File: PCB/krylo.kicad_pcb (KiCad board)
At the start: 2 copper layers, 135.3 x 87.6 mm, 51 parts, among them SW1 Switch, SW10 Switch, SW11 Switch, SW12 Switch, SW13 Switch, SW14 Switch, SW15 Switch, SW16 Switch, SW2 Switch, SW3 Switch, SW4 Switch, SW5 Switch, SW6 Switch, SW7 Switch, SW8 Switch, SW9 Switch, U1 nice_nano

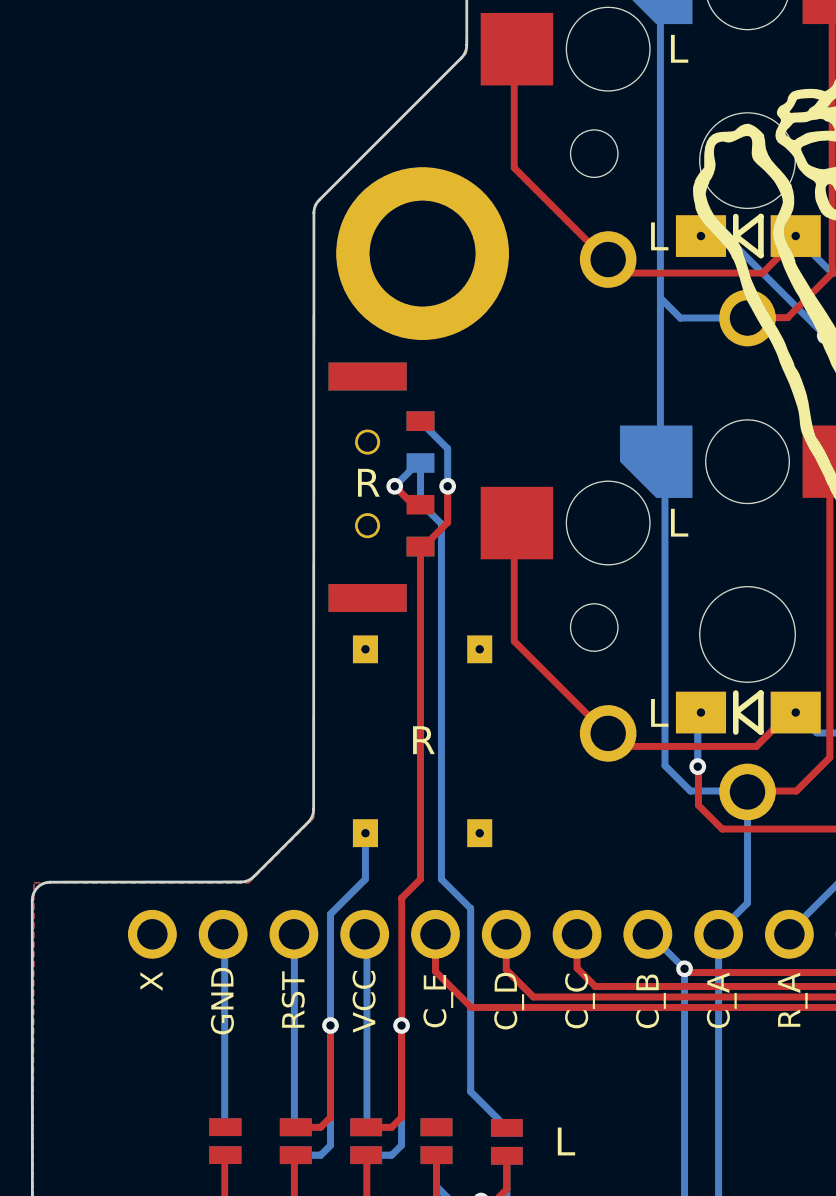
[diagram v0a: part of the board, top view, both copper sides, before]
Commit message: Repositioned the reset button and the mount point to make them a bit more centered relative to the resulting area
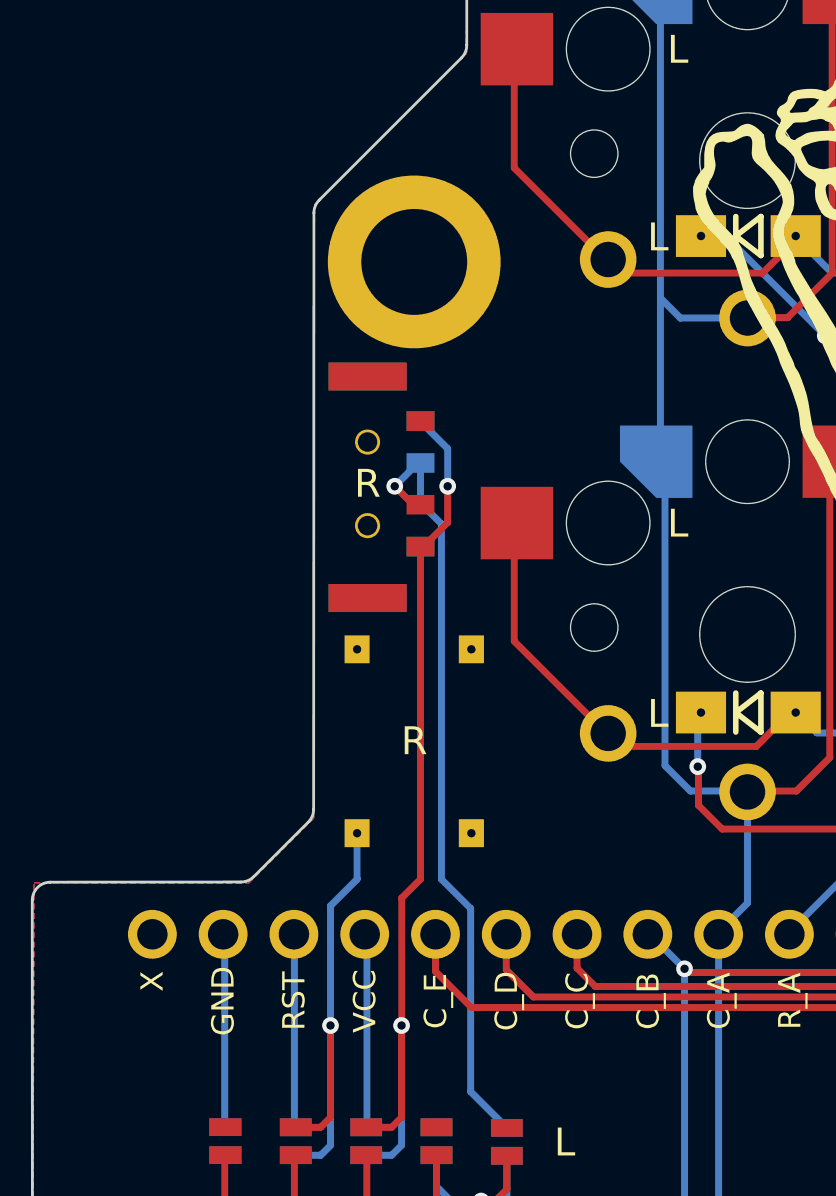
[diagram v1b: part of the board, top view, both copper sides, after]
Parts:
- moved H4 0.42 mm to (105.0, 74.2)
- moved RESET1 0.30 mm to (105.0, 91.4)
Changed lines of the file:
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@@
 		(fp_poly
 			(pts
-				(xy -8.75 -8.250001) (xy 8.75 -8.25) (xy 8.75 8.250001) (xy -8.75 8.25)
+				(xy -8.75 -8.250002) (xy 8.75 -8.25) (xy 8.75 8.250002) (xy -8.75 8.25)
 			)
 			(stroke
@@
 		(fp_poly
 			(pts
-				(xy -8.75 -8.250001) (xy 8.75 -8.25) (xy 8.75 8.250001) (xy -8.75 8.25)
+				(xy -8.75 -8.250002) (xy 8.75 -8.25) (xy 8.75 8.250002) (xy -8.75 8.25)
 			)
 			(stroke
@@
 		(fp_line
 			(start 2.5 -1.5)
-			(end 7.000001 -1.5)
+			(end 7.000002 -1.5)
 			(stroke
 				(width 0.1)
@@
 		)
 		(fp_line
-			(start 7.000001 -1.5)
+			(start 7.000002 -1.5)
 			(end 7 -6.2)
 			(stroke
@@
 		)
 		(fp_line
-			(start -9.55 -2.499999)
+			(start -9.55 -2.499998)
 			(end -7 -2.5)
 			(stroke
@@
 		(fp_line
 			(start -9.55 -5)
-			(end -9.55 -2.499999)
+			(end -9.55 -2.499998)
 			(stroke
 				(width 0.1)
@@
 		)
 		(fp_line
-			(start 4.549999 -5.957)
+			(start 4.549998 -5.957)
 			(end 4.55 -7.228)
 			(stroke
@@
 		)
 		(fp_line
-			(start -9.549999 -2.5)
+			(start -9.549998 -2.5)
 			(end -7 -2.5)
 			(stroke
@@
 		(fp_line
 			(start -9.55 -5)
-			(end -9.549999 -2.5)
+			(end -9.549998 -2.5)
 			(stroke
 				(width 0.1)
@@
 		)
 		(fp_line
-			(start -9.549999 -2.5)
+			(start -9.549998 -2.5)
 			(end -7 -2.5)
 			(stroke
@@
 		(fp_line
 			(start -9.55 -5)
-			(end -9.549999 -2.5)
+			(end -9.549998 -2.5)
 			(stroke
 				(width 0.1)
@@
 		)
 		(fp_line
-			(start -9.549999 -2.5)
+			(start -9.549998 -2.5)
 			(end -7 -2.5)
 			(stroke
@@
 		(fp_line
 			(start -9.55 -5)
-			(end -9.549999 -2.5)
+			(end -9.549998 -2.5)
 			(stroke
 				(width 0.1)
@@
 		(fp_line
 			(start -2 -7.7)
-			(end -1.5 -8.200001)
+			(end -1.5 -8.200002)
 			(stroke
 				(width 0.1)
@@
 		)
 		(fp_line
-			(start -1.5 -8.200001)
+			(start -1.5 -8.200002)
 			(end 1.5 -8.2)
 			(stroke
@@
 		(fp_line
 			(start 7 -5)
-			(end 9.55 -4.999999)
+			(end 9.55 -4.999998)
 			(stroke
 				(width 0.1)
@@
 		)
 		(fp_line
-			(start 9.55 -4.999999)
+			(start 9.55 -4.999998)
 			(end 9.55 -2.5)
 			(stroke
@@
 		)
 		(fp_line
-			(start -1.5 -8.200001)
+			(start -1.5 -8.200002)
 			(end -2 -7.7)
 			(stroke
@@
 		(fp_line
 			(start 1.5 -8.2)
-			(end -1.5 -8.200001)
+			(end -1.5 -8.200002)
 			(stroke
 				(width 0.1)
@@
 		)
 		(fp_line
-			(start 1.999999 -4.25)
+			(start 1.999998 -4.25)
 			(end 2 -7.7)
 			(stroke
@@
 		(fp_line
 			(start 4.54 -5.95)
-			(end 3.281 -4.690999)
+			(end 3.281 -4.690998)
 			(stroke
 				(width 0.1)
@@
 	(footprint "krylo:Mount"
 		(layer "F.Cu")
-		(at 105.3 73.9)
+		(at 105 74.2)
 		(property "Reference" "H4"
 			(at 0 -2.5 0)
@@
 	(footprint "krylo:ResetSW"
 		(layer "F.Cu")
-		(at 105.3 91.4 -90)
+		(at 105 91.4 -90)
 		(descr "tactile push button, 6x6mm e.g. PTS645xx series, height=9.5mm")
 		(tags "tact sw push 6mm smd")
@@
 				(polygon
 					(pts
-						(xy 105.37209 90.79822) (xy 105.434574 90.81107) (xy 105.488983 90.831495) (xy 105.538795 90.860676)
-						(xy 105.579725 90.896447) (xy 105.612753 90.939206) (xy 105.636843 90.987586) (xy 105.651679 91.04217)
-						(xy 105.656839 91.104314) (xy 105.651307 91.169119) (xy 105.635164 91.227962) (xy 105.608539 91.282001)
-						(xy 105.572257 91.329736) (xy 105.528931 91.367188) (xy 105.477747 91.395268) (xy 105.670821 91.815)
-						(xy 105.442821 91.815) (xy 105.277713 91.428852) (xy 105.179771 91.428852) (xy 105.179771 91.815)
-						(xy 104.972714 91.815) (xy 104.972714 91.247013) (xy 105.179771 91.247013) (xy 105.300122 91.247013)
-						(xy 105.345474 91.242672) (xy 105.380867 91.230735) (xy 105.408505 91.212025) (xy 105.429415 91.186381)
-						(xy 105.44235 91.154369) (xy 105.446973 91.114084) (xy 105.442312 91.071869) (xy 105.429331 91.038512)
-						(xy 105.408505 91.01199) (xy 105.380756 90.992472) (xy 105.345361 90.980089) (xy 105.300122 90.975598)
-						(xy 105.179771 90.975598) (xy 105.179771 91.247013) (xy 104.972714 91.247013) (xy 104.972714 90.793698)
-						(xy 105.300122 90.793698)
+						(xy 105.07209 90.79822) (xy 105.134574 90.81107) (xy 105.188983 90.831495) (xy 105.238795 90.860676)
+						(xy 105.279725 90.896447) (xy 105.312753 90.939206) (xy 105.336843 90.987586) (xy 105.351679 91.04217)
+						(xy 105.356839 91.104314) (xy 105.351307 91.169119) (xy 105.335164 91.227962) (xy 105.308539 91.282001)
+						(xy 105.272257 91.329736) (xy 105.228931 91.367188) (xy 105.177747 91.395268) (xy 105.370821 91.815)
+						(xy 105.142821 91.815) (xy 104.977713 91.428852) (xy 104.879771 91.428852) (xy 104.879771 91.815)
+						(xy 104.672714 91.815) (xy 104.672714 91.247013) (xy 104.879771 91.247013) (xy 105.000122 91.247013)
+						(xy 105.045474 91.242672) (xy 105.080867 91.230735) (xy 105.108505 91.212025) (xy 105.129415 91.186381)
+						(xy 105.14235 91.154369) (xy 105.146973 91.114084) (xy 105.142312 91.071869) (xy 105.129331 91.038512)
+						(xy 105.108505 91.01199) (xy 105.080756 90.992472) (xy 105.045361 90.980089) (xy 105.000122 90.975598)
+						(xy 104.879771 90.975598) (xy 104.879771 91.247013) (xy 104.672714 91.247013) (xy 104.672714 90.793698)
+						(xy 105.000122 90.793698)
 					)
 				)
@@
 				(polygon
 					(pts
-						(xy 105.558714 91.814999) (xy 105.558714 90.793697) (xy 105.348848 90.793697) (xy 105.348848 91.626138)
-						(xy 104.936139 91.626138) (xy 104.936139 91.814999)
+						(xy 105.258714 91.814999) (xy 105.258714 90.793697) (xy 105.048848 90.793697) (xy 105.048848 91.626138)
+						(xy 104.636139 91.626138) (xy 104.636139 91.814999)
 					)
 				)
@@
 		(fp_line
 			(start -0.45 -0.7)
-			(end -0.45 0.700001)
+			(end -0.45 0.700002)
 			(stroke
 				(width 0.2)
@@
 		(fp_line
 			(start -0.45 0)
-			(end 0.45 -0.700001)
+			(end 0.45 -0.700002)
 			(stroke
 				(width 0.2)
@@
 		)
 		(fp_line
-			(start 0.45 -0.700001)
+			(start 0.45 -0.700002)
 			(end 0.45 0.7)
 			(stroke
@@
 		(fp_line
 			(start -0.45 -0.7)
-			(end -0.45 0.700001)
+			(end -0.45 0.700002)
 			(stroke
 				(width 0.2)
@@
 		(fp_line
 			(start -0.45 0)
-			(end 0.45 -0.700001)
+			(end 0.45 -0.700002)
 			(stroke
 				(width 0.2)
@@
 		)
 		(fp_line
-			(start 0.45 -0.700001)
+			(start 0.45 -0.700002)
 			(end 0.45 0.7)
 			(stroke
@@
 		(fp_poly
 			(pts
-				(xy -8.75 -8.250001) (xy 8.75 -8.25) (xy 8.75 8.250001) (xy -8.75 8.25)
+				(xy -8.75 -8.250002) (xy 8.75 -8.25) (xy 8.75 8.250002) (xy -8.75 8.25)
 			)
 			(stroke
@@
 		(fp_poly
 			(pts
-				(xy -8.75 -8.250001) (xy 8.75 -8.25) (xy 8.75 8.250001) (xy -8.75 8.25)
+				(xy -8.75 -8.250002) (xy 8.75 -8.25) (xy 8.75 8.250002) (xy -8.75 8.25)
 			)
 			(stroke
@@
 		(fp_line
 			(start 2.5 -1.5)
-			(end 7.000001 -1.5)
+			(end 7.000002 -1.5)
 			(stroke
 				(width 0.1)
@@
 		)
 		(fp_line
-			(start 7.000001 -1.5)
+			(start 7.000002 -1.5)
 			(end 7 -6.2)
 			(stroke
@@
 		)
 		(fp_line
-			(start -9.55 -2.499999)
+			(start -9.55 -2.499998)
 			(end -7 -2.5)
 			(stroke
@@
 		(fp_line
 			(start -9.55 -5)
-			(end -9.55 -2.499999)
+			(end -9.55 -2.499998)
 			(stroke
 				(width 0.1)
@@
 		)
 		(fp_line
-			(start 4.549999 -5.957)
+			(start 4.549998 -5.957)
 			(end 4.55 -7.228)
 			(stroke
@@
 		(fp_line
 			(start -1.5 -3.7)
-			(end 0.999999 -3.7)
+			(end 0.999998 -3.7)
 			(stroke
 				(width 0.1)
@@
 		)
 		(fp_arc
-			(start 0.999999 -3.7)
+			(start 0.999998 -3.7)
 			(mid 2.06066 -3.26066)
 			(end 2.5 -2.2)
@@
 		(fp_poly
 			(pts
-				(xy -8.75 -8.250001) (xy 8.75 -8.25) (xy 8.75 8.250001) (xy -8.75 8.25)
+				(xy -8.75 -8.250002) (xy 8.75 -8.25) (xy 8.75 8.250002) (xy -8.75 8.25)
 			)
 			(stroke
@@
 		(fp_poly
 			(pts
-				(xy -8.75 -8.250001) (xy 8.75 -8.25) (xy 8.75 8.250001) (xy -8.75 8.25)
+				(xy -8.75 -8.250002) (xy 8.75 -8.25) (xy 8.75 8.250002) (xy -8.75 8.25)
 			)
 			(stroke
@@
 		(fp_line
 			(start 2.5 -1.5)
-			(end 7.000001 -1.5)
+			(end 7.000002 -1.5)
 			(stroke
 				(width 0.1)
@@
 		)
 		(fp_line
-			(start 7.000001 -1.5)
+			(start 7.000002 -1.5)
 			(end 7 -6.2)
 			(stroke
@@
 		)
 		(fp_line
-			(start -9.55 -2.499999)
+			(start -9.55 -2.499998)
 			(end -7 -2.5)
 			(stroke
@@
 		(fp_line
 			(start -9.55 -5)
-			(end -9.55 -2.499999)
+			(end -9.55 -2.499998)
 			(stroke
 				(width 0.1)
@@
 		)
 		(fp_line
-			(start 4.549999 -5.957)
+			(start 4.549998 -5.957)
 			(end 4.55 -7.228)
 			(stroke
@@
 	)
 	(segment
-		(start 101.995243 105.904757)
-		(end 101.644815 106.255185)
+		(start 102.95 94.7)
+		(end 102.95 96.352)
+		(width 0.25)
+		(layer "B.Cu")
+		(net "RESET")
+	)
+	(segment
+		(start 102 101.595243)
+		(end 101.995243 101.6)
 		(width 0.25)
 		(layer "B.Cu")
@@
 	)
 	(segment
-		(start 103.25 96.352)
-		(end 101.995243 97.606757)
+		(start 101.995243 105.904757)
+		(end 101.644815 106.255185)
 		(width 0.25)
 		(layer "B.Cu")
@@
 	)
 	(segment
-		(start 101.995243 97.604757)
-		(end 101.995243 101.6)
+		(start 102.95 96.352)
+		(end 101.995243 97.306757)
 		(width 0.25)
 		(layer "B.Cu")
@@
 	)
 	(segment
-		(start 103.25 94.7)
-		(end 103.25 96.35)
+		(start 101.995243 97.306757)
+		(end 101.995243 101.6)
 		(width 0.25)
 		(layer "B.Cu")

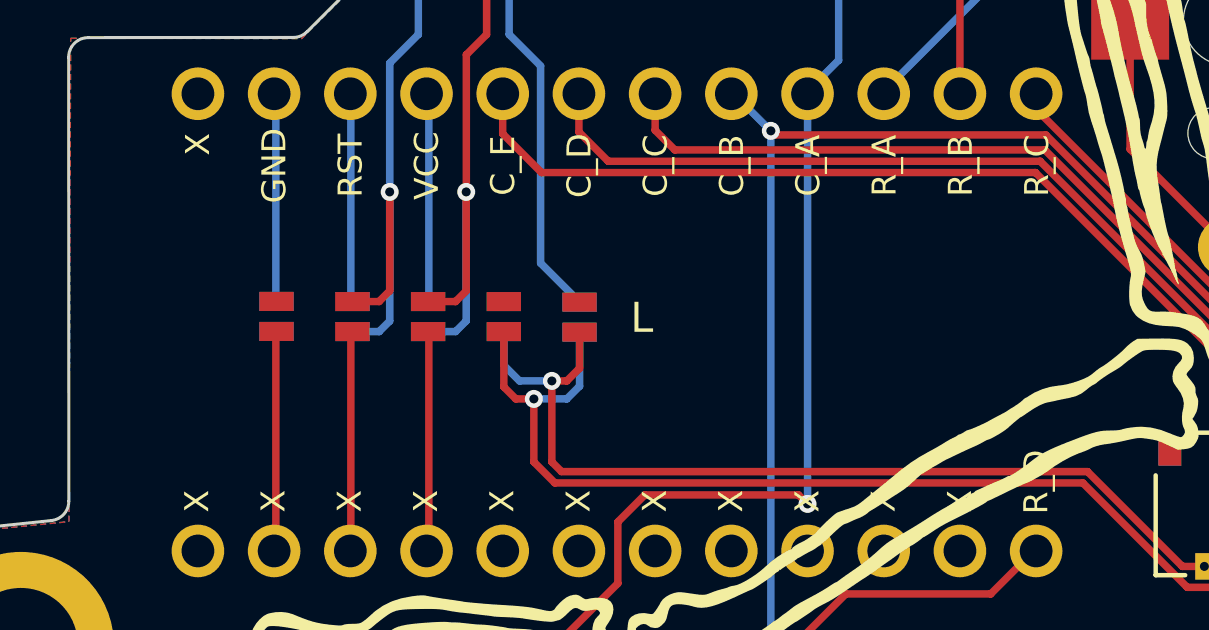
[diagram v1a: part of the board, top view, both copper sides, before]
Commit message: Metadata info silkscreen print added
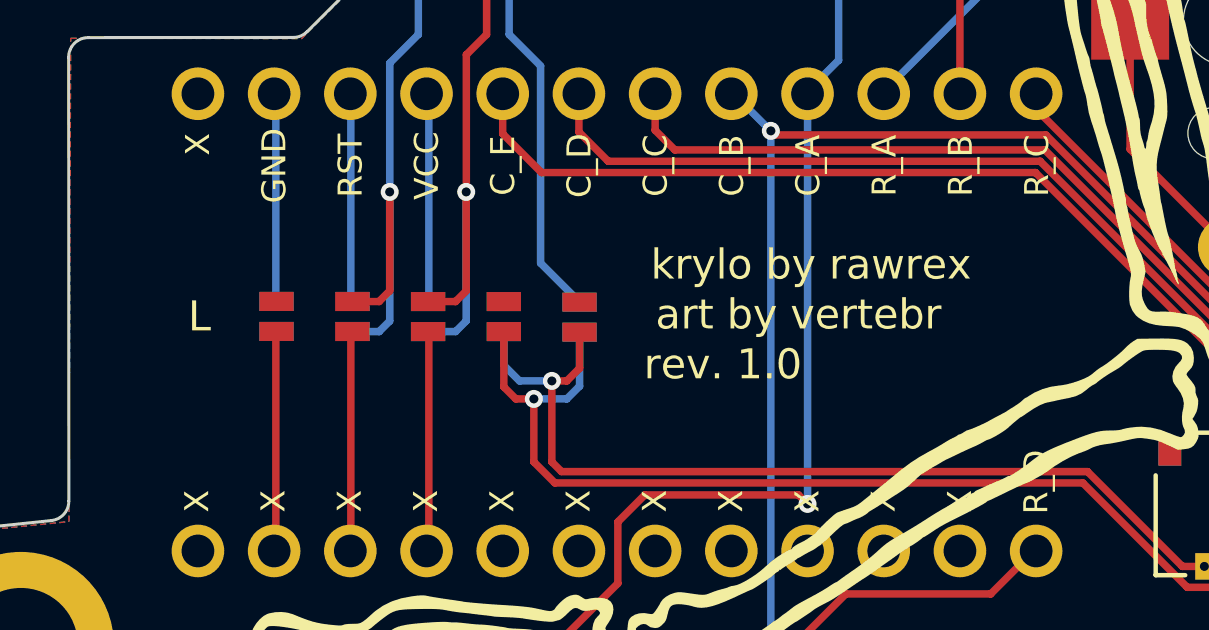
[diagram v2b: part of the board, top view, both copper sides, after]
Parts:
- added INFO: Info, krylo:Info, F.Cu at (115.5, 105.3)
- BT1: value MOLEX_C -> Molex
- H1, H2, H3, H4: value Mount -> SMTSO2020MTJ_M2

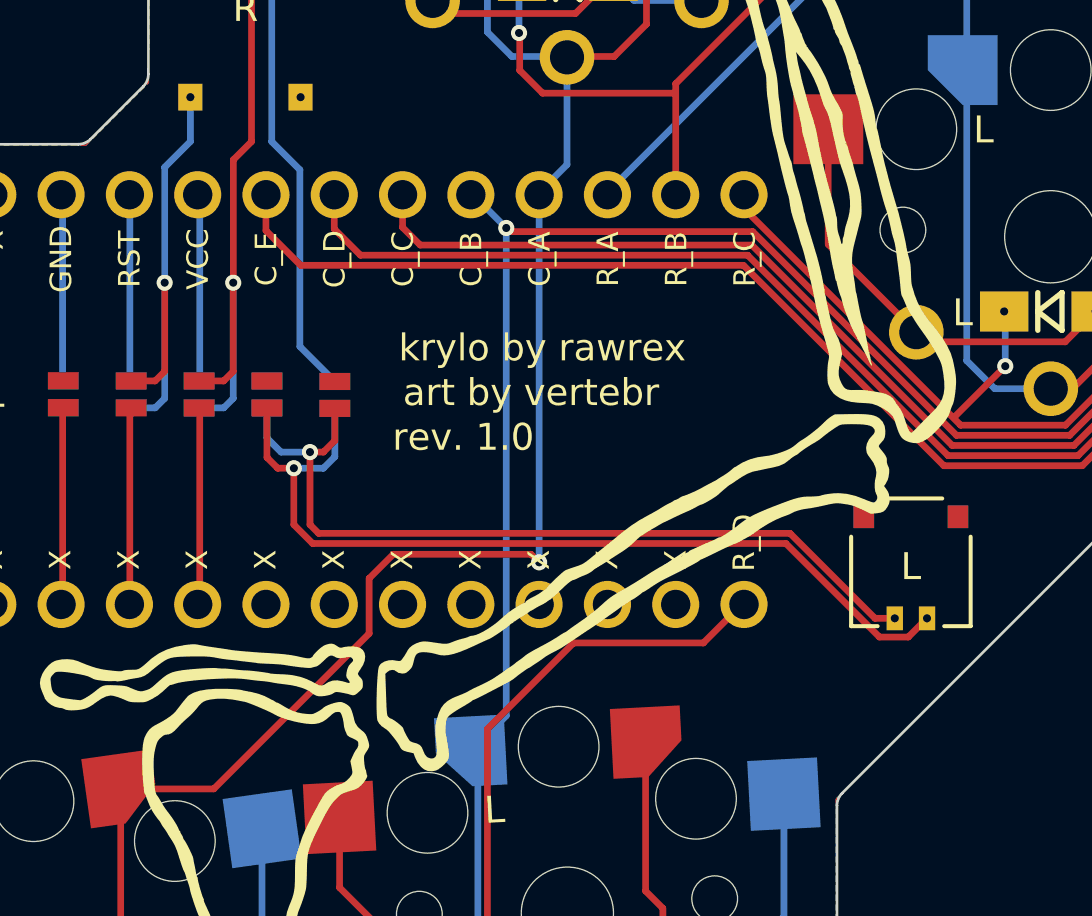
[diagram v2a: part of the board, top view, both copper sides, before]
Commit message: Jumpers placement correction
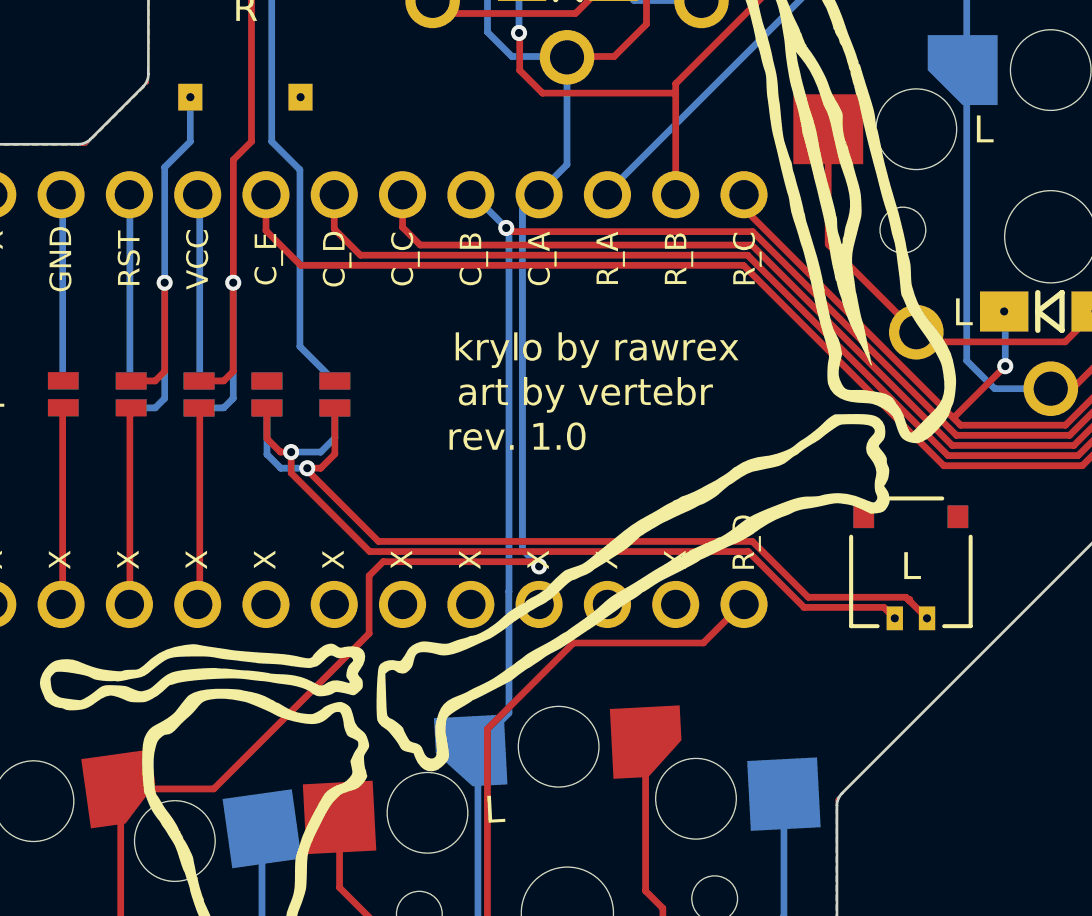
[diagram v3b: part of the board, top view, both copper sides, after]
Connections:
- JP1 pad 1: /PAD2 -> /PAD1
- JP2 pad 1: /PAD2 -> /PAD1
- JP3 pad 1: /PAD1 -> /PAD2
- JP4 pad 1: /PAD1 -> /PAD2
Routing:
- net /PAD1: track 34.2 -> 31.8 mm
- net col_A: track 131.1 -> 131.7 mm
